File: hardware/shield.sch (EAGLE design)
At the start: 7 parts, among them U1 ARDUINOR3-DIMENSION, X1 22-23-2021

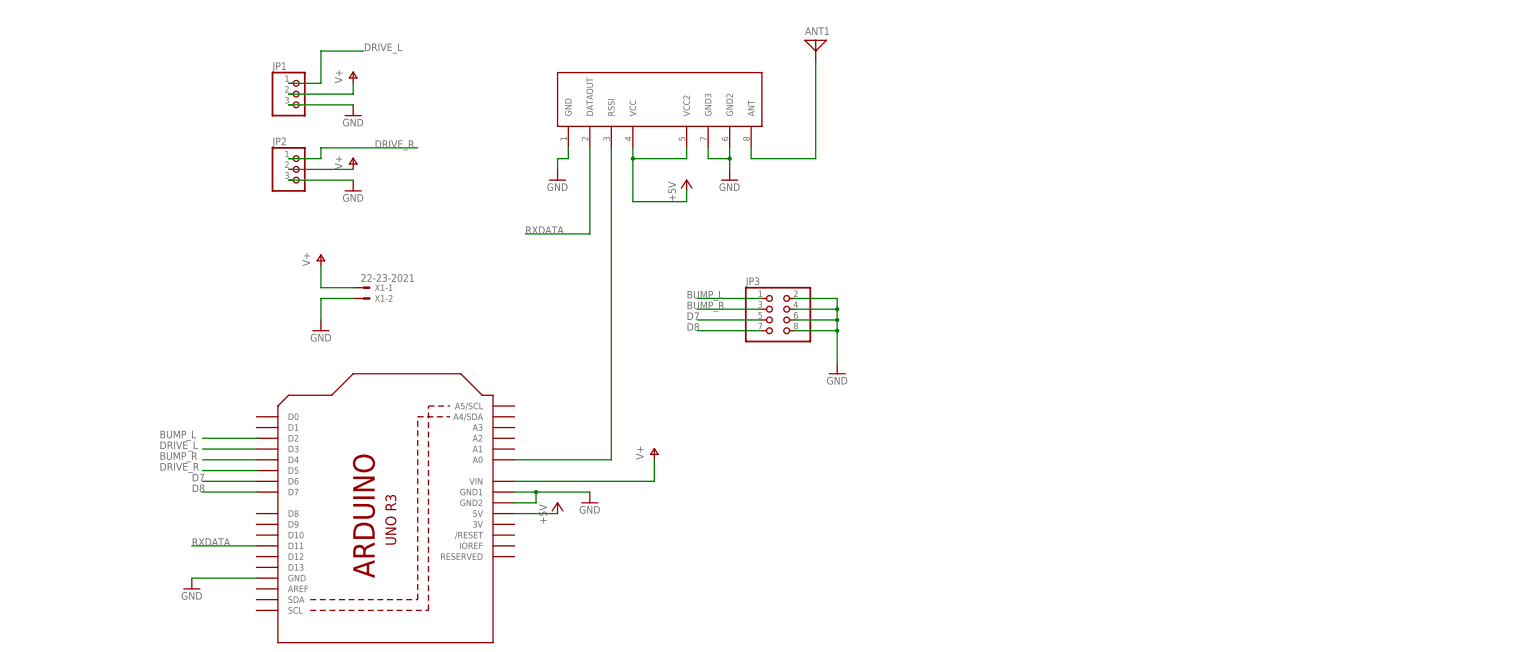
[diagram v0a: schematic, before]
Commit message: add bluetoothdevice to schematic
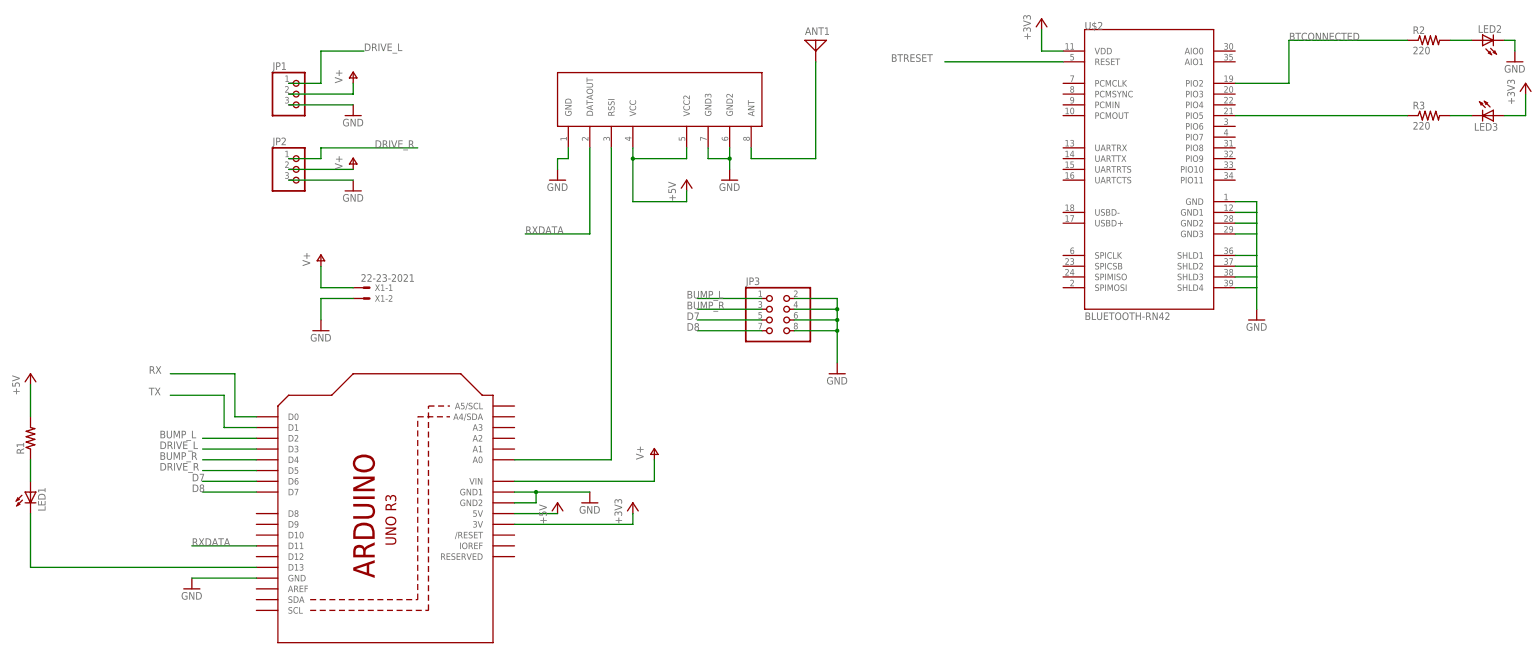
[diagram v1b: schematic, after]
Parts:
- added LED1, LED2, LED3: (no value), led:LED3MM
- added R1: (no value), resistor:R-US_R0805
- added R2, R3: 220, resistor:R-US_R0805
- added U$2: BLUETOOTH-RN42, RN4x:BLUETOOTH-RN42
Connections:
- new net +3V3: LED3.A, U$2.VDD, U1.3V
- new net BTCONNECTED: R2.1, U$2.PIO2
- new net BTRESET: U$2.RESET
- new net N$2: LED1.A, R1.1
- new net N$3: LED1.C, U1.D13
- new net N$5: LED2.A, R2.2
- new net N$7: LED3.C, R3.2
- new net N$8: R3.1, U$2.PIO5
- new net RX: U1.D0
- new net TX: U1.D1
- net +5V: now also R1.2
- net GND: now also LED2.C, U$2.GND, U$2.GND1, U$2.GND2, U$2.GND3, U$2.SHLD1, U$2.SHLD2, U$2.SHLD3, U$2.SHLD4
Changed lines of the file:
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@@
 <part name="JP3" library="adafruit" deviceset="PINHD-2X4" device=""/>
 <part name="GND8" library="supply1" deviceset="GND" device=""/>
+<part name="U$2" library="RN4x" deviceset="BLUETOOTH-RN42" device=""/>
+<part name="LED1" library="led" deviceset="LED" device="3MM"/>
+<part name="R1" library="resistor" deviceset="R-US_" device="R0805"/>
+<part name="P+7" library="supply1" deviceset="+5V" device=""/>
+<part name="LED2" library="led" deviceset="LED" device="3MM"/>
+<part name="LED3" library="led" deviceset="LED" device="3MM"/>
+<part name="GND9" library="supply1" deviceset="GND" device=""/>
+<part name="GND10" library="supply1" deviceset="GND" device=""/>
+<part name="+3V1" library="supply1" deviceset="+3V3" device=""/>
+<part name="+3V2" library="supply1" deviceset="+3V3" device=""/>
+<part name="+3V3" library="supply1" deviceset="+3V3" device=""/>
+<part name="R2" library="resistor" deviceset="R-US_" device="R0805" value="220"/>
+<part name="R3" library="resistor" deviceset="R-US_" device="R0805" value="220"/>
 </parts>
 <sheets>
@@
 <instance part="JP3" gate="A" x="106.68" y="88.9"/>
 <instance part="GND8" gate="1" x="121.92" y="76.2"/>
+<instance part="U$2" gate="G$1" x="182.88" y="132.08"/>
+<instance part="LED1" gate="G$1" x="-68.58" y="48.26"/>
+<instance part="R1" gate="G$1" x="-68.58" y="60.96" rot="R90"/>
+<instance part="P+7" gate="1" x="-68.58" y="76.2"/>
+<instance part="LED2" gate="G$1" x="274.32" y="154.94" rot="R90"/>
+<instance part="LED3" gate="G$1" x="276.86" y="137.16" rot="R270"/>
+<instance part="GND9" gate="1" x="220.98" y="88.9"/>
+<instance part="GND10" gate="1" x="281.94" y="149.86"/>
+<instance part="+3V1" gate="G$1" x="170.18" y="160.02"/>
+<instance part="+3V2" gate="G$1" x="284.48" y="144.78"/>
+<instance part="+3V3" gate="G$1" x="73.66" y="45.72"/>
+<instance part="R2" gate="G$1" x="261.62" y="154.94"/>
+<instance part="R3" gate="G$1" x="261.62" y="137.16"/>
 </instances>
 <busses>
@@
 <pinref part="JP3" gate="A" pin="8"/>
 </segment>
+<segment>
+<pinref part="U$2" gate="G$1" pin="GND"/>
+<wire x1="215.9" y1="116.84" x2="220.98" y2="116.84" width="0.1524" layer="91"/>
+<pinref part="GND9" gate="1" pin="GND"/>
+<wire x1="220.98" y1="116.84" x2="220.98" y2="114.3" width="0.1524" layer="91"/>
+<pinref part="U$2" gate="G$1" pin="GND1"/>
+<wire x1="220.98" y1="114.3" x2="220.98" y2="111.76" width="0.1524" layer="91"/>
+<wire x1="220.98" y1="111.76" x2="220.98" y2="109.22" width="0.1524" layer="91"/>
+<wire x1="220.98" y1="109.22" x2="220.98" y2="104.14" width="0.1524" layer="91"/>
+<wire x1="220.98" y1="104.14" x2="220.98" y2="101.6" width="0.1524" layer="91"/>
+<wire x1="220.98" y1="101.6" x2="220.98" y2="99.06" width="0.1524" layer="91"/>
+<wire x1="220.98" y1="99.06" x2="220.98" y2="96.52" width="0.1524" layer="91"/>
+<wire x1="220.98" y1="96.52" x2="220.98" y2="91.44" width="0.1524" layer="91"/>
+<wire x1="215.9" y1="114.3" x2="220.98" y2="114.3" width="0.1524" layer="91"/>
+<pinref part="U$2" gate="G$1" pin="GND2"/>
+<wire x1="215.9" y1="111.76" x2="220.98" y2="111.76" width="0.1524" layer="91"/>
+<pinref part="U$2" gate="G$1" pin="GND3"/>
+<wire x1="215.9" y1="109.22" x2="220.98" y2="109.22" width="0.1524" layer="91"/>
+<pinref part="U$2" gate="G$1" pin="SHLD1"/>
+<wire x1="215.9" y1="104.14" x2="220.98" y2="104.14" width="0.1524" layer="91"/>
+<pinref part="U$2" gate="G$1" pin="SHLD2"/>
+<wire x1="215.9" y1="101.6" x2="220.98" y2="101.6" width="0.1524" layer="91"/>
+<pinref part="U$2" gate="G$1" pin="SHLD3"/>
+<wire x1="215.9" y1="99.06" x2="220.98" y2="99.06" width="0.1524" layer="91"/>
+<pinref part="U$2" gate="G$1" pin="SHLD4"/>
+<wire x1="215.9" y1="96.52" x2="220.98" y2="96.52" width="0.1524" layer="91"/>
+</segment>
+<segment>
+<pinref part="LED2" gate="G$1" pin="C"/>
+<wire x1="279.4" y1="154.94" x2="281.94" y2="154.94" width="0.1524" layer="91"/>
+<pinref part="GND10" gate="1" pin="GND"/>
+<wire x1="281.94" y1="154.94" x2="281.94" y2="152.4" width="0.1524" layer="91"/>
+</segment>
 </net>
 <net name="N$4" class="0">
@@
 <junction x="73.66" y="127"/>
 </segment>
+<segment>
+<pinref part="R1" gate="G$1" pin="2"/>
+<wire x1="-68.58" y1="66.04" x2="-68.58" y2="73.66" width="0.1524" layer="91"/>
+<pinref part="P+7" gate="1" pin="+5V"/>
+</segment>
 </net>
 <net name="DRIVE_L" class="0">
@@
 </segment>
 </net>
+<net name="RX" class="0">
+<segment>
+<pinref part="U1" gate="G$1" pin="D0"/>
+<wire x1="-15.24" y1="66.04" x2="-20.32" y2="66.04" width="0.1524" layer="91"/>
+<wire x1="-20.32" y1="66.04" x2="-20.32" y2="76.2" width="0.1524" layer="91"/>
+<wire x1="-20.32" y1="76.2" x2="-35.56" y2="76.2" width="0.1524" layer="91"/>
+<label x="-40.64" y="76.2" size="1.778" layer="95"/>
+</segment>
+</net>
+<net name="TX" class="0">
+<segment>
+<pinref part="U1" gate="G$1" pin="D1"/>
+<wire x1="-15.24" y1="63.5" x2="-22.86" y2="63.5" width="0.1524" layer="91"/>
+<wire x1="-22.86" y1="63.5" x2="-22.86" y2="71.12" width="0.1524" layer="91"/>
+<wire x1="-22.86" y1="71.12" x2="-35.56" y2="71.12" width="0.1524" layer="91"/>
+<label x="-40.64" y="71.12" size="1.778" layer="95"/>
+</segment>
+</net>
+<net name="N$2" class="0">
+<segment>
+<pinref part="R1" gate="G$1" pin="1"/>
+<pinref part="LED1" gate="G$1" pin="A"/>
+<wire x1="-68.58" y1="55.88" x2="-68.58" y2="50.8" width="0.1524" layer="91"/>
+</segment>
+</net>
+<net name="N$3" class="0">
+<segment>
+<pinref part="LED1" gate="G$1" pin="C"/>
+<wire x1="-68.58" y1="43.18" x2="-68.58" y2="30.48" width="0.1524" layer="91"/>
+<pinref part="U1" gate="G$1" pin="D13"/>
+<wire x1="-68.58" y1="30.48" x2="-15.24" y2="30.48" width="0.1524" layer="91"/>
+</segment>
+</net>
+<net name="BTCONNECTED" class="0">
+<segment>
+<pinref part="U$2" gate="G$1" pin="PIO2"/>
+<wire x1="215.9" y1="144.78" x2="228.6" y2="144.78" width="0.1524" layer="91"/>
+<wire x1="228.6" y1="144.78" x2="228.6" y2="154.94" width="0.1524" layer="91"/>
+<pinref part="R2" gate="G$1" pin="1"/>
+<wire x1="256.54" y1="154.94" x2="228.6" y2="154.94" width="0.1524" layer="91"/>
+<label x="228.6" y="154.94" size="1.778" layer="95"/>
+</segment>
+</net>
+<net name="+3V3" class="0">
+<segment>
+<pinref part="+3V3" gate="G$1" pin="+3V3"/>
+<pinref part="U1" gate="G$1" pin="3V"/>
+<wire x1="73.66" y1="43.18" x2="73.66" y2="40.64" width="0.1524" layer="91"/>
+<wire x1="73.66" y1="40.64" x2="45.72" y2="40.64" width="0.1524" layer="91"/>
+</segment>
+<segment>
+<pinref part="+3V2" gate="G$1" pin="+3V3"/>
+<pinref part="LED3" gate="G$1" pin="A"/>
+<wire x1="284.48" y1="142.24" x2="284.48" y2="137.16" width="0.1524" layer="91"/>
+<wire x1="284.48" y1="137.16" x2="279.4" y2="137.16" width="0.1524" layer="91"/>
+</segment>
+<segment>
+<pinref part="U$2" gate="G$1" pin="VDD"/>
+<pinref part="+3V1" gate="G$1" pin="+3V3"/>
+<wire x1="175.26" y1="152.4" x2="170.18" y2="152.4" width="0.1524" layer="91"/>
+<wire x1="170.18" y1="152.4" x2="170.18" y2="157.48" width="0.1524" layer="91"/>
+</segment>
+</net>
+<net name="N$5" class="0">
+<segment>
+<pinref part="R2" gate="G$1" pin="2"/>
+<pinref part="LED2" gate="G$1" pin="A"/>
+<wire x1="266.7" y1="154.94" x2="271.78" y2="154.94" width="0.1524" layer="91"/>
+</segment>
+</net>
+<net name="N$7" class="0">
+<segment>
+<pinref part="R3" gate="G$1" pin="2"/>
+<pinref part="LED3" gate="G$1" pin="C"/>
+<wire x1="266.7" y1="137.16" x2="271.78" y2="137.16" width="0.1524" layer="91"/>
+</segment>
+</net>
+<net name="N$8" class="0">
+<segment>
+<pinref part="R3" gate="G$1" pin="1"/>
+<pinref part="U$2" gate="G$1" pin="PIO5"/>
+<wire x1="256.54" y1="137.16" x2="215.9" y2="137.16" width="0.1524" layer="91"/>
+</segment>
+</net>
+<net name="BTRESET" class="0">
+<segment>
+<pinref part="U$2" gate="G$1" pin="RESET"/>
+<wire x1="175.26" y1="149.86" x2="147.32" y2="149.86" width="0.1524" layer="91"/>
+<label x="134.62" y="149.86" size="1.778" layer="95"/>
+</segment>
+</net>
